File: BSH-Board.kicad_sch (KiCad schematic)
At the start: 58 parts, among them J1 667101210103, J2 MICRO QTZB5.0, Q1 MMST3904, SW1 TS-3025-B-C-B, SW2 TS-3025-B-C-B, U1 ESP32-C6-MINI-1-N4, U2 AP63203WU, U5 74LVC1G07, U6 74LVC1G17

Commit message: Finished layout
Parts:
- renumbered C7 to C1, C8 to C2, C1 to C3, C2 to C4, C3 to C5, C4 to C6, C9 to C7, C10 to C8, D5 to D2, D4 to D3, D7 to D4, D6 to D5, D9 to D6, D3 to D7, R14 to R1, R3 to R10, R4 to R11, R5 to R12, R12 to R2, R11 to R3, R13 to R4, R15 to R5, R7 to R6, R8 to R7, R9 to R8, R2 to R9, SW2 to SW1, SW1 to SW2, TP4 to TP1, TP11 to TP10, TP12 to TP11, TP21 to TP12, TP22 to TP13, TP13 to TP14, TP14 to TP15, TP15 to TP16, TP16 to TP17, TP17 to TP18, TP18 to TP19, TP3 to TP2, TP19 to TP20, TP20 to TP21, TP1 to TP3, TP2 to TP4, TP8 to TP7, TP9 to TP8, TP10 to TP9, U5 to U1, U6 to U2, U2 to U3, U1 to U4

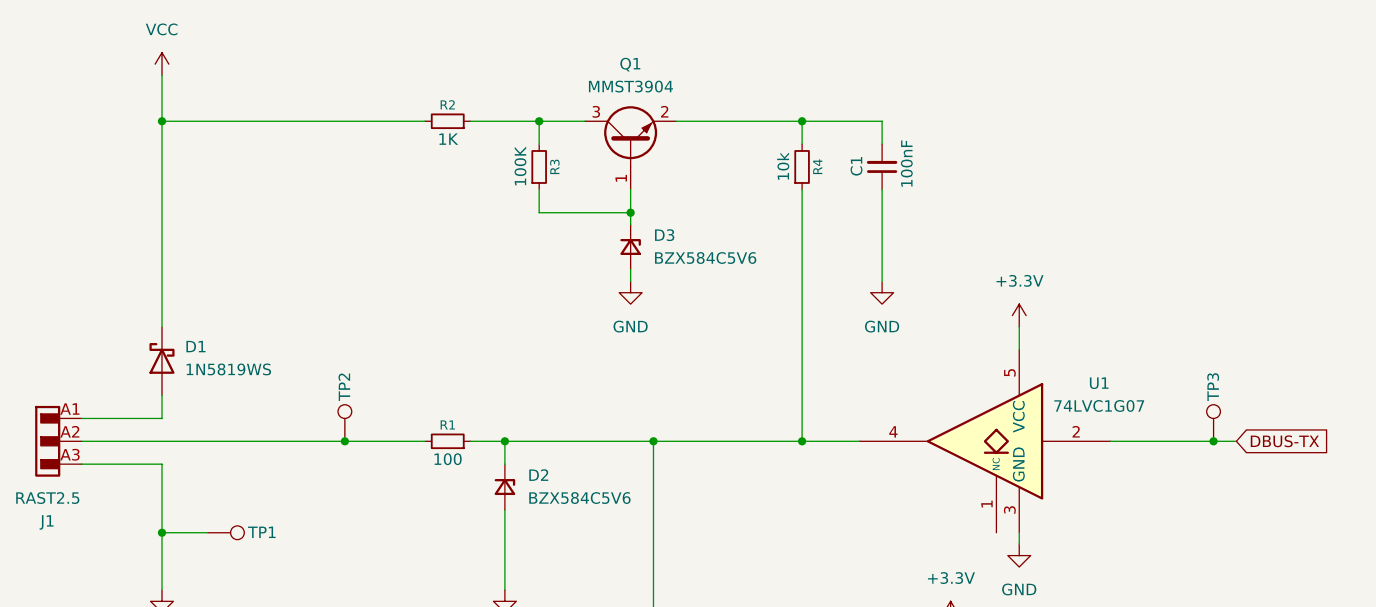
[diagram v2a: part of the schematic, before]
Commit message: Add dip switch for pullup, add TX pullup, add empty 0805 for potential other pullup value
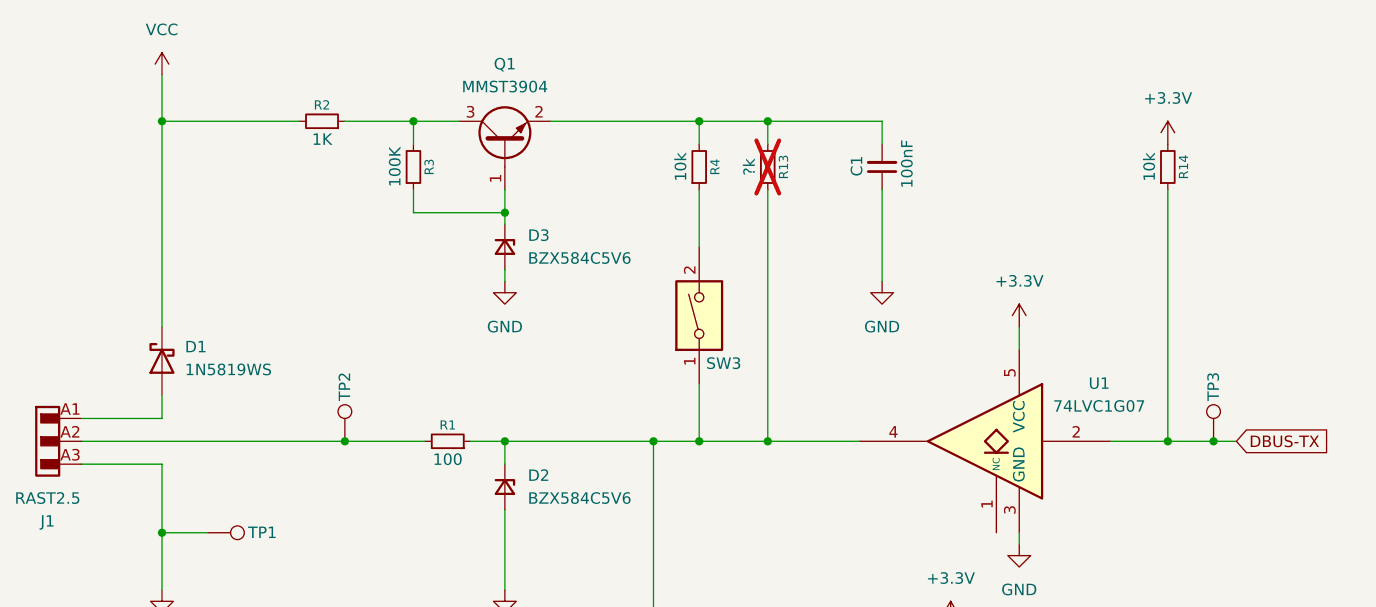
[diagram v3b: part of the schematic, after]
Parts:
- added R13: ?k, Resistor_SMD:R_0805_2012Metric_Pad1.20x1.40mm_HandSolder, symbol Device:R_Small
- added R14: 10k, Resistor_SMD:R_0402_1005Metric, symbol Device:R_Small
- added SW3: SW_DIP_x01, footprints:SW-SMD_DSHP01TSGER, symbol Switch:SW_DIP_x01
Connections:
- net +3.3V: now also R14.2
- net DBUS-TX: now also R14.1
- net at D2.1 (K), R1.1, R5.2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: now also R13.1, SW3.1; no longer R4.1
- net at C1.2, Q1.2 (E), R4.2: now also R13.2
- new net: R4.1, SW3.2
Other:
- moved on the sheet: D3, Q1, R2, R3, R4

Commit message: Various minor improvements
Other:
- moved on the sheet: C3, C4, C5, C6, C7, C8, D4, D5, D6, D7, J2, L1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

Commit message: Hopefully fixed output now
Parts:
- SW3: LCSC (none) -> C3293141
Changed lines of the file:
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@@
+			)
+		)
+		(property "LCSC" "C3293141"
+			(at 99.06 60.96 90)
+			(effects
+				(font
+					(size 1.27 1.27)
+				)
+				(hide yes)
 			)
 		)
